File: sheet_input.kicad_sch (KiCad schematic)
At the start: 23 parts, among them J1 NCJ6FA-H, J5 VDD_PoE / PGND, Q1 DMP3098 (P-FET 60V), SW1 SS-12D00-G3

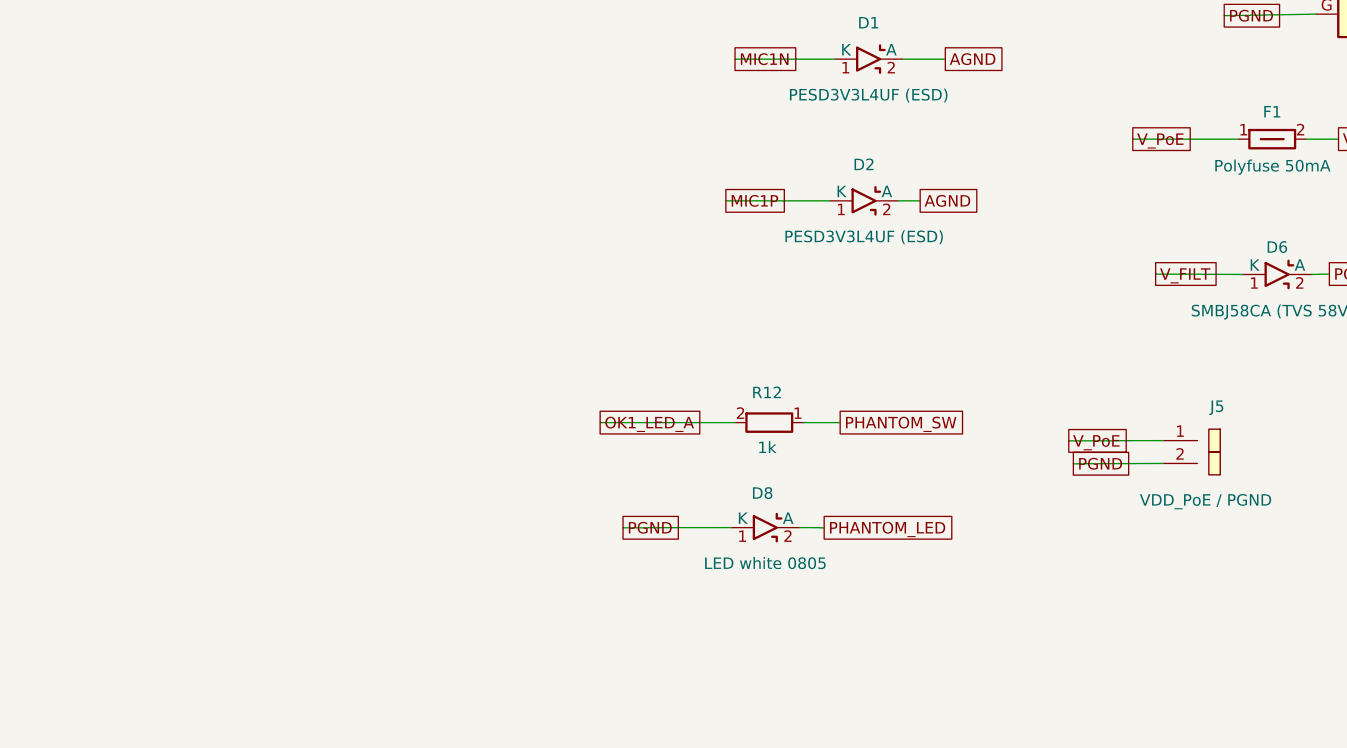
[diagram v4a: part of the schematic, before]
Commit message: feat: phantom PoE-tap disconnect via SPDT + dual PhotoMOS
Open both PoE-tap lines (V_PoE and PGND) when phantom is off so the
Ethernet-referenced PoE ground stops coupling buzz into a dynamic mic.
SW1 (SPDT) drives the Q1 enable plus two KAQY214S PhotoMOS SSRs (K1/K2)
through R17/R18: K1 breaks V_PoE, K2 breaks PGND. Both lines must open
because C17 (100nF) bridges them, so breaking one alone leaves the buzz.

SMD PhotoMOS instead of a DPDT slide: the through-hole DPDT's pads cut
through the inner-layer I2S/I2C bus (33 DRC shorts); the SOP-4 SSRs sit
on one copper layer and route clean.

sheet_input: SW1 back to SPDT; add K1/K2 (scramble_hat:PhotoMOS symbol,
  KiCad SOP-4_3.8x4.1 footprint) + R17/R18 470R; J5 -> TAP_HV/TAP_GND.
BOM: SW1 SS-12D00-G3, K1/K2 KAQY214S (C2890344), R17/R18 (C114877).
PCB: place + route new parts; correct bottom-side 3D-model rotations
  (180 deg on the mirror-fixed parts U1/OK1/Q1/D2/D6/D7/D8); restore
  exclude_from_pos_files on J1/J2/J5/C19 that a re-layout had wiped
  (they were leaking into the CPL).
fab: regenerate gerbers/drill/BOM/CPL (52 placed; excludes C19/J1/J2/J5/R14).
Remove the now-unused DPDT footprint + 3D model.

Verify K1/K2 (SOP-4, -90) and U1 (QFN, +270) rotations in the JLCPCB
assembly preview before ordering.
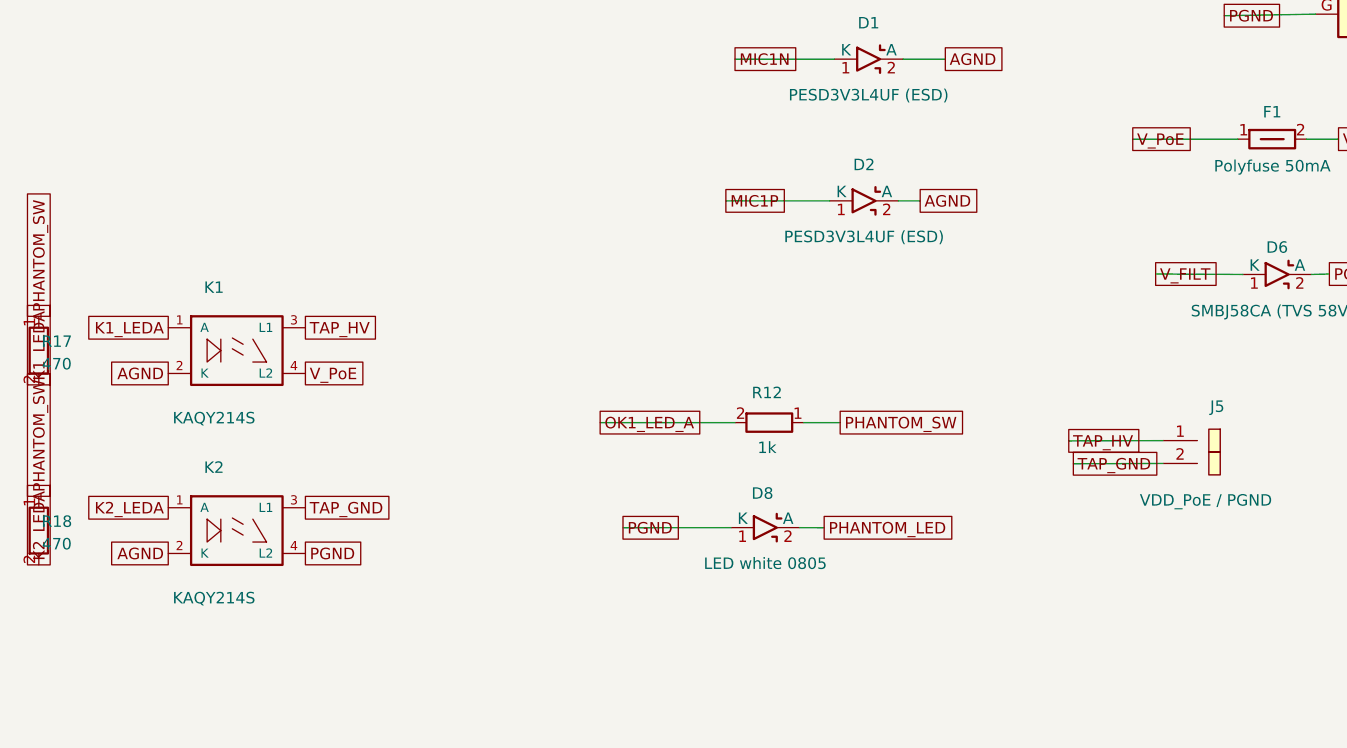
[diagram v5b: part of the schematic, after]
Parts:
- added K1, K2: KAQY214S, Package_SO:SOP-4_3.8x4.1mm_P2.54mm, symbol scramble_hat:PhotoMOS
- added R17, R18: 470, Resistor_SMD:R_0402_1005Metric, symbol scramble_hat:R
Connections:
- net AGND: now also K1.2 (K), K2.2 (K)
- net PGND: now also K2.4 (L2); no longer J5.2 (Pin_2)
- net PHANTOM_SW: now also R17.1, R18.1
- net V_PoE: now also K1.4 (L2); no longer J5.1 (Pin_1)
- new net K1_LEDA: K1.1 (A), R17.2
- new net K2_LEDA: K2.1 (A), R18.2
- new net TAP_GND: J5.2 (Pin_2), K2.3 (L1)
- new net TAP_HV: J5.1 (Pin_1), K1.3 (L1)

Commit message: feat: auto-detect Hi-Z guitar input (buffer + 4053 mux on MIC1)
Add a high-impedance electric-guitar input that shares the codec's MIC1
channel with the XLR mic and switches over automatically when a 1/4"
plug is inserted.

- Detect: the 1/4" jack is a TRS socket, so a mono guitar (TS) plug
  shorts the Ring to Sleeve/PGND. Ring pulled to +5V (R19) + debounce
  (C27) => DET low = "instrument".
- Buffer U3 (TLV9061, +5V): ~1M input on the jack tip, unity follower;
  the codec PGA provides the level so no extra stage is needed. R20/R21
  input, R22/R23+C24 mid-rail bias, R24/C25 output.
- Mux U4 (74HC4053, +5V): dual-SPDT picks the MIC1P/MIC1N source = XLR
  mic (no plug) or buffered guitar + PGND ref (plug). Pseudo-differential:
  guitar-mode cold reference = PGND, so the codec rejects the PGND/AGND
  ground noise -- stays clean even with phantom left on.
- The mux sits on the CODEC side of C10/C11: the XLR side carries up to
  57V phantom (via R5/R6), which the coupling caps block from the 5V
  switch. Confirmed no 48V path to the guitar or the switch/buffer.
- Splices: C10.2 -> MIC1P_XLR, C11.2 -> MIC1N_XLR (now the mux commons);
  J1 T -> GTIP, J1 R -> DET; ESD D1/D2 relocated to the XLR far plates
  to clamp the mux inputs.

Parts LCSC-verified in stock (~$0.50/board + 2 extended feeders).
Schematic + BOM only; not on the board yet -- F8 + place + route for the
next rev. U4 is TSSOP-16 with no CPL rotation pattern; verify its
rotation in the JLCPCB assembly preview before ordering.
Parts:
- added C23: 0.22uF, Capacitor_SMD:C_0402_1005Metric, symbol scramble_hat:C
- added C24: 4.7uF, Capacitor_SMD:C_0603_1608Metric, symbol scramble_hat:C
- added C25, C26: 1uF, Capacitor_SMD:C_0402_1005Metric, symbol scramble_hat:C
- added C27, C28, C29: 100nF, Capacitor_SMD:C_0402_1005Metric, symbol scramble_hat:C
- added R19: 100k, Resistor_SMD:R_0402_1005Metric, symbol scramble_hat:R
- added R20: 2.2k, Resistor_SMD:R_0402_1005Metric, symbol scramble_hat:R
- added R21: 1M, Resistor_SMD:R_0402_1005Metric, symbol scramble_hat:R
- added R22, R23: 220k, Resistor_SMD:R_0402_1005Metric, symbol scramble_hat:R
- added R24: 100, Resistor_SMD:R_0402_1005Metric, symbol scramble_hat:R
- added U3: TLV9061, Package_TO_SOT_SMD:SOT-23-5, symbol scramble_hat:Opamp_Single
- added U4: 74HC4053, Package_SO:TSSOP-16_4.4x5mm_P0.65mm, symbol scramble_hat:SW_4053
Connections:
- net AGND: now also C24.2, C27.2, C28.2, C29.2, R23.2, U3.2 (V-), U4.6 (Inh), U4.7 (VEE), U4.8 (VSS), U4.9 (C)
- net MIC1N: now also U4.15 (Y); no longer C11.2, D1.1 (K)
- net MIC1P: now also U4.14 (X); no longer C10.2, D2.1 (K)
- net PGND: now also C26.1
- net unconnected-(J1-JACK_R-PadR) renamed DET
- net DET: now also C27.1, R19.2, U4.10 (B), U4.11 (A)
- net unconnected-(J1-JACK_T-PadT) renamed GTIP
- net GTIP: now also C23.1
- new net +5V: C28.1, C29.1, R19.1, R22.1, U3.5 (V+), U4.16 (VDD)
- new net BUF_AC: C25.2, U4.12 (X0)
- new net BUF_OUT: R24.1, U3.1 (OUT), U3.4 (-)
- new net BUF_R: C25.1, R24.2
- new net GB_IN: R20.2, R21.1, U3.3 (+)
- new net GB_N: C23.2, R20.1
- new net MIC1N_XLR: C11.2, D1.1 (K), U4.1 (Y1)
- new net MIC1P_XLR: C10.2, D2.1 (K), U4.13 (X1)
- new net PGND_AC: C26.2, U4.2 (Y0)
- new net VBIAS: C24.1, R21.2, R22.2, R23.1

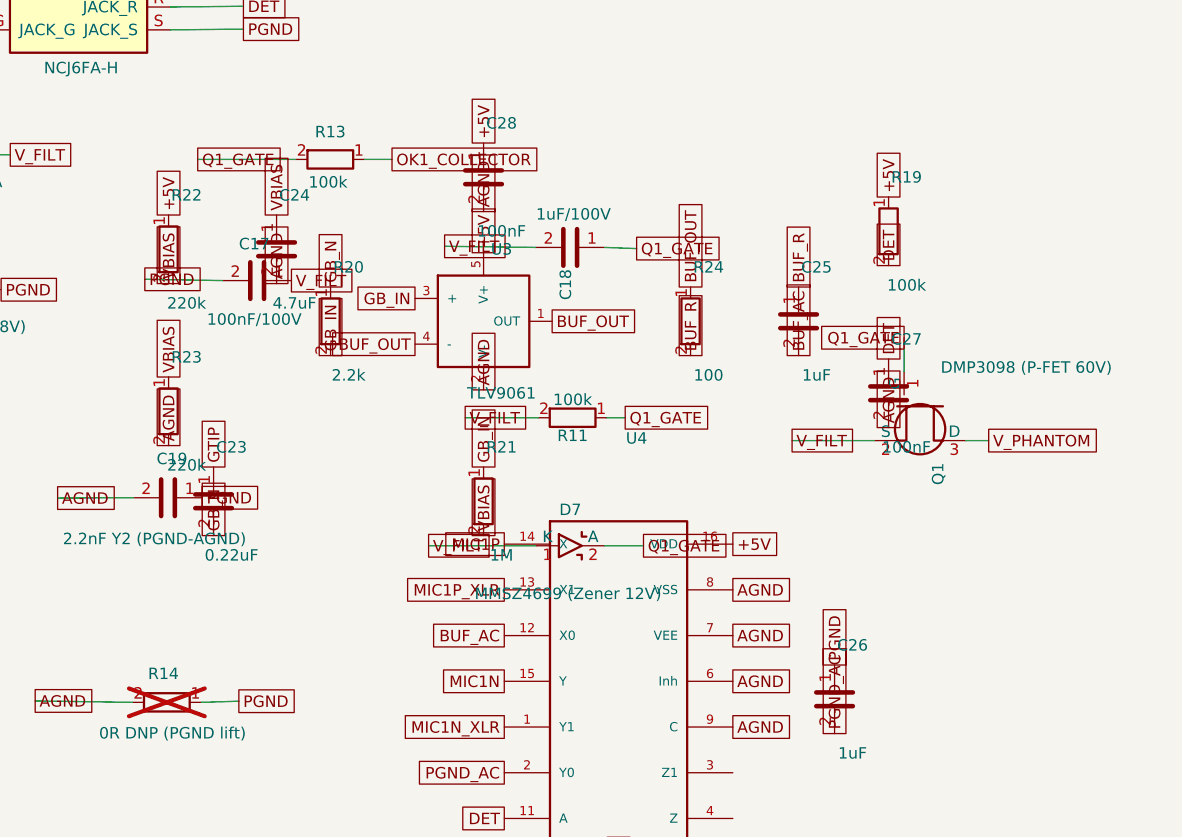
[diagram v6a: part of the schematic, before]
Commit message: fix: guitar-input detect ground path; consolidate values; add tip ESD
The ring-detect as first committed could not work with phantom off: the
hat's PGND (XLR shield, jack sleeve) reaches AGND only through
capacitors (C19) and the DNP R14, so it floats at DC and the detect
pull-up would drag the whole net high instead of reading the plug's
ring-to-sleeve short. Add R25 (10k PGND->AGND bleed) to give the detect
a DC return; DET now reads ~0.45V with a plug in. Side benefit: the XLR
shield is no longer floating when the PoE tap is open (it now bleeds to
audio ground), without recreating the low-impedance tap loop the
PhotoMOS disconnect exists to break.

Also:
- Consolidate new-block values onto reels already in the BOM: C23/C24
  0.22uF/4.7uF -> 1uF (fc 0.16Hz and -44dB rail filtering both still
  fine), R22/R23 220k -> 100k, R24 100R -> 33R. The rev now adds a
  single new passive value (1M) and four BOM rows total.
- R26 (1M GTIP->AGND): pre-biases C23 so plug insertion doesn't pop and
  defines the tip DC level; input impedance becomes ~500k (1M || 1M).
- D9 (TPD1E10B06, X1-SON-2): bidirectional +/-5.5V 12pF ESD clamp on
  the exposed tip contact, returned to PGND (the shield), so strikes
  don't dump through audio ground. Unidirectional 3.3V spares on D1/D2
  were unsuitable (would clip negative guitar peaks).
- gitignore __pycache__/.

Netlist re-verified: no shorts; drift vs PCB = exactly the 18 new parts
+ 6 splices. Parts LCSC-verified in stock (D9 C48260, ~100k stock).
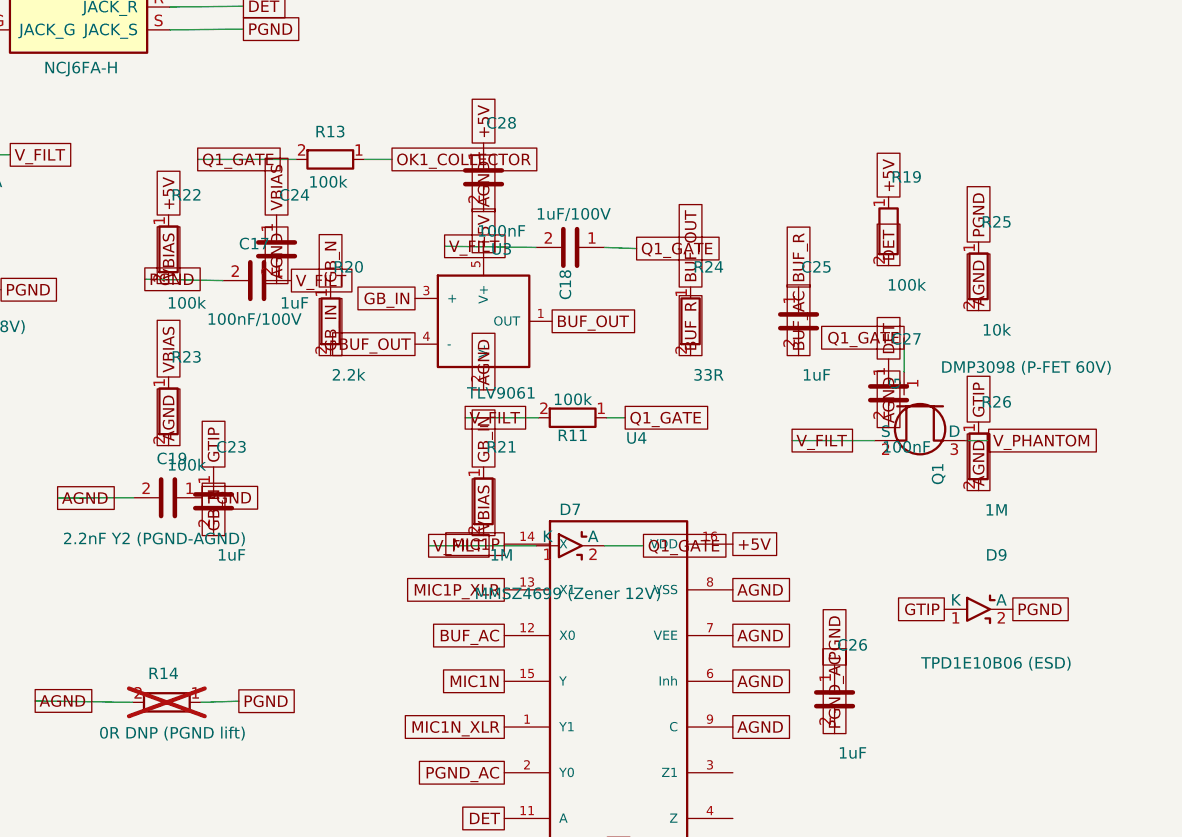
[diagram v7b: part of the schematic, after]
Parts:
- added D9: TPD1E10B06 (ESD), Package_SON:Texas_DPY0002A_0.6x1mm_P0.65mm, symbol scramble_hat:D_TVS
- added R25: 10k, Resistor_SMD:R_0402_1005Metric, symbol scramble_hat:R
- added R26: 1M, Resistor_SMD:R_0402_1005Metric, symbol scramble_hat:R
- C23: value 0.22uF -> 1uF
- C24: value 4.7uF -> 1uF; footprint Capacitor_SMD:C_0603_1608Metric -> Capacitor_SMD:C_0402_1005Metric
- R22, R23: value 220k -> 100k
- R24: value 100 -> 33R
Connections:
- net AGND: now also R25.2, R26.2
- net GTIP: now also D9.1 (K), R26.1
- net PGND: now also D9.2 (A), R25.1
